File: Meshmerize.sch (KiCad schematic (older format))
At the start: 45 parts, among them M1 Motor_DC, M2 Motor_DC, SW1 SW_Push, U1 LM324, U2 ESP32-DEVKITC-32D, U3 TCRT5000, U4 TCRT5000, U5 MT3608, U6 TCRT5000, U7 TCRT5000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

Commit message: Completed PCB Routing
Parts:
- removed SW1: SW_Push, Button_Switch_THT:SW_PUSH_6mm, symbol Switch:SW_Push
- added H1, H2, H3, H4: MountingHole, MountingHole:MountingHole_2.2mm_M2, symbol Mechanical:MountingHole
- added J1, J2: Conn_01x19_Male, Connector_PinHeader_2.54mm:PinHeader_1x19_P2.54mm_Vertical, symbol Connector:Conn_01x19_Male
- added J3: Conn_01x04_Female, Connector_PinSocket_2.54mm:PinSocket_1x04_P2.54mm_Vertical, symbol Connector:Conn_01x04_Female
- added S2: MPB04-2C33-S-D, MPB04-2C33-S-D:SW_MPB04-2C33-S-D, symbol Meshmerize-rescue:MPB04-2C33-S-D-MPB04-2C33-S-D
- D6: symbol SS34:SS34 -> Meshmerize-rescue:SS34-SS34
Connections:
- net labels added: SCL_OLED, SDA_OLED
- wire segments 162 -> 201
- no-connect marks 22 -> 4

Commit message: Optimized schematics, routing and performed clean up
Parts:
- U5: symbol Regulator_Switching:MT3608 -> Meshmerize-rescue:MT3608-Regulator_Switching
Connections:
- wire segments 201 -> 203
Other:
- note added: "Buffer Op. Amplifiers - IC LM 324"
- note added: "Debug Switch"
- note added: "Indication LEDs"
- note added: "MCU - ESP 32"
- note added: "MT3608 - Boost StepUp Voltage Reg"
- note added: "Meshmerize"
- note added: "Motor Driver - TB6612FNG"
- note added: "Mounting Holes"
- note added: "OLED Port"
- note added: "Power Switch"
- note added: "TCRT5000 - IR TX RX"
- note removed: "LM342_Op-Amp\n"
- note removed: "POWER_CIRCUITARY\n"
- note removed: "TB6612FNG_Motor_Driver\n\n"
- moved on the sheet: BT2, C1, C2, D1, D2, D3, D4, D5, D6, H1, H2, H3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

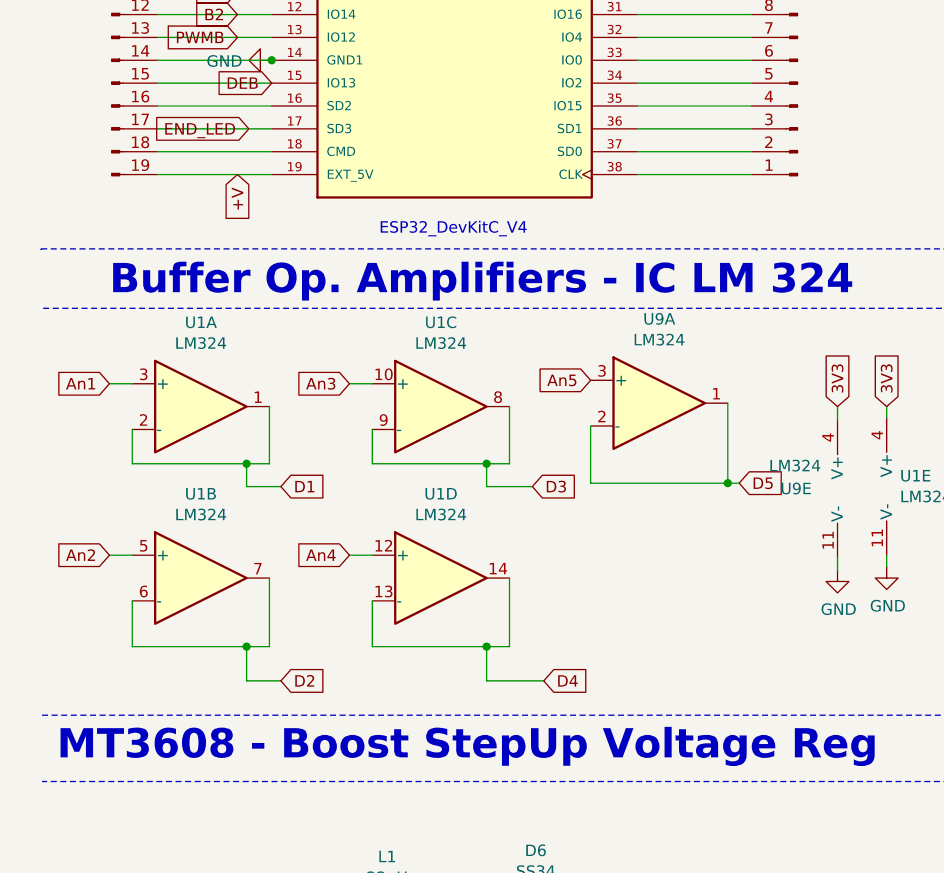
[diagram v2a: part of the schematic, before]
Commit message: Added R-Pot for LSA sensitivity, jumper to power ESP32 using inbuilt regulator, minor optimizations
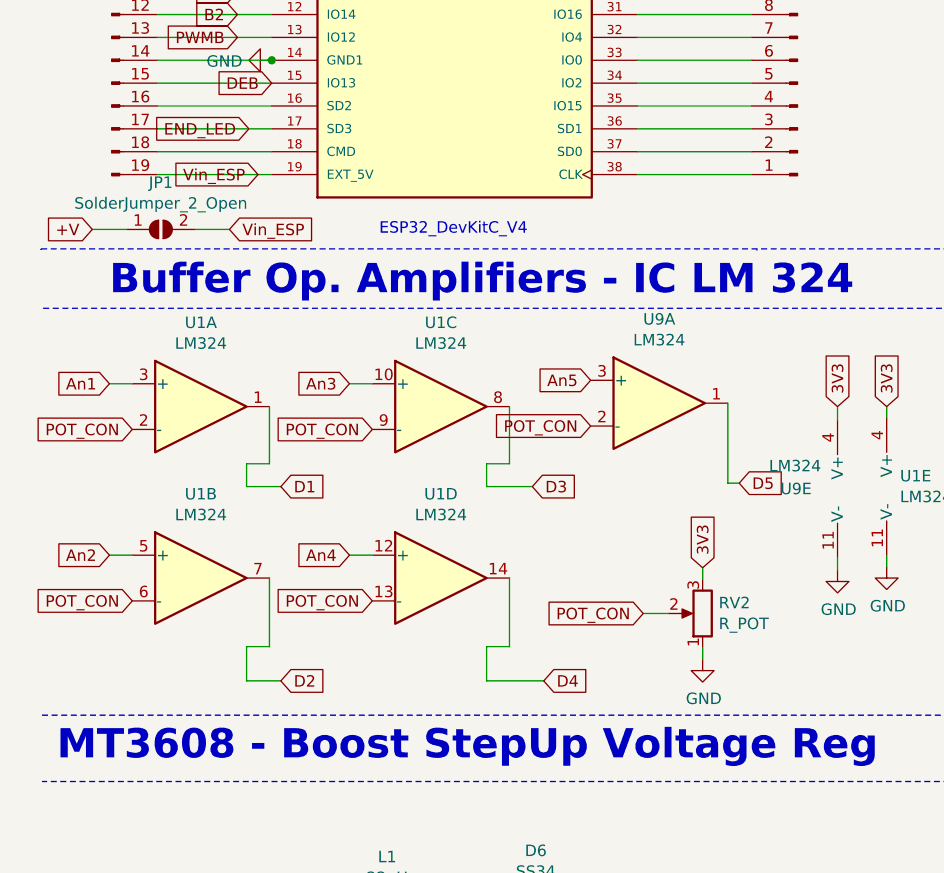
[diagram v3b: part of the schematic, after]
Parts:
- added JP1: SolderJumper_2_Open, Jumper:SolderJumper-2_P1.3mm_Open_Pad1.0x1.5mm, symbol Jumper:SolderJumper_2_Open
- added RV2: R_POT, 3296W-1-202LF:TRIM_3296W-1-202LF, symbol Device:R_POT
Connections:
- net +V: now also JP1.1 (A); no longer J1.19 (Pin_19), U2.19 (EXT_5V)
- net 3V3: now also RV2.3
- net D1: no longer U1.2 (-)
- net D2: no longer U1.6 (-)
- net D3: no longer U1.9 (-)
- net D4: no longer U1.13 (-)
- net D5: no longer U9.2 (-)
- net GND: now also RV2.1
- new net POT_CON: RV2.2, U1.13 (-), U1.2 (-), U1.6 (-), U1.9 (-), U9.2 (-)
- new net Vin_ESP: J1.19 (Pin_19), JP1.2 (B), U2.19 (EXT_5V)
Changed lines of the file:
@@
 $EndComp
-Wire Wire Line
-	865  4185 865  4335
-Wire Wire Line
-	865  4335 1365 4335
 Wire Wire Line
 	1465 4335 1465 4085
 Wire Wire Line
-	1915 4185 1915 4335
-Wire Wire Line
-	1915 4335 2415 4335
-Wire Wire Line
 	2515 4335 2515 4085
 Wire Wire Line
 	1465 4835 1465 5135
 Wire Wire Line
-	865  5135 865  4935
-Wire Wire Line
 	2515 4835 2515 5135
 Wire Wire Line
 	2515 5135 2415 5135
-Wire Wire Line
-	1915 5135 1915 4935
 $Comp
 L power:GND #PWR0120
@@
 Wire Wire Line
 	2415 4435 2615 4435
-Connection ~ 2415 4335
 Wire Wire Line
 	2415 4335 2515 4335
@@
 Wire Wire Line
 	1365 4435 1515 4435
-Connection ~ 1365 4335
 Wire Wire Line
 	1365 4335 1465 4335
@@
 	1365 5285 1515 5285
 Wire Wire Line
-	865  5135 1365 5135
-Connection ~ 1365 5135
-Wire Wire Line
 	1365 5135 1465 5135
 Wire Wire Line
@@
 Wire Wire Line
 	2415 5285 2665 5285
-Connection ~ 2415 5135
-Wire Wire Line
-	2415 5135 1915 5135
 Text GLabel 765  3985 0    50   Input ~ 0
 An1
@@
 $EndComp
 Wire Wire Line
-	2870 4170 2870 4420
-Wire Wire Line
-	2870 4420 3470 4420
-Wire Wire Line
 	3470 4420 3470 4070
 Text GLabel 2870 3970 0    50   Input ~ 0
@@
 Wire Wire Line
 	3470 4420 3520 4420
-Connection ~ 3470 4420
 $Comp
 L power:GND #PWR02
@@
 	975  2770 1475 2770
 Wire Wire Line
-	975  3070 1475 3070
-Wire Wire Line
 	975  1270 1475 1270
 $Comp
@@
 Text GLabel 1475 2670 0    50   Input ~ 0
 DEB
-Text GLabel 1325 3070 3    50   Input ~ 0
+Text GLabel 690  3310 0    50   Input ~ 0
 +V
 Text GLabel 1375 1270 1    50   Input ~ 0
@@
 Wire Notes Line
 	8295 2490 11200 2490
+$Comp
+L Device:R_POT RV2
+U 1 1 6199FDC2
+P 3360 4990
+F 0 "RV2" H 3290 4944 50  0000 R CNN
+F 1 "R_POT" H 3290 5035 50  0000 R CNN
+F 2 "3296W-1-202LF:TRIM_3296W-1-202LF" H 3360 4990 50  0001 C CNN
+F 3 "~" H 3360 4990 50  0001 C CNN
+	1    3360 4990
+	-1   0    0    1
+$EndComp
+Text GLabel 3100 4990 0    50   Input ~ 0
+POT_CON
+Wire Wire Line
+	3210 4990 3100 4990
+$Comp
+L power:GND #PWR0107
+U 1 1 619F79F0
+P 3360 5190
+F 0 "#PWR0107" H 3360 4940 50  0001 C CNN
+F 1 "GND" H 3365 5017 50  0000 C CNN
+F 2 "" H 3360 5190 50  0001 C CNN
+F 3 "" H 3360 5190 50  0001 C CNN
+	1    3360 5190
+	1    0    0    -1
+$EndComp
+Wire Wire Line
+	3360 5140 3360 5190
+Wire Wire Line
+	3360 4840 3360 4790
+Text GLabel 3360 4790 1    50   Input ~ 0
+3V3
+Text GLabel 2870 4170 0    50   Input ~ 0
+POT_CON
+Text GLabel 1915 4185 0    50   Input ~ 0
+POT_CON
+Text GLabel 865  4185 0    50   Input ~ 0
+POT_CON
+Text GLabel 865  4935 0    50   Input ~ 0
+POT_CON
+Text GLabel 1915 4935 0    50   Input ~ 0
+POT_CON
+Text GLabel 1290 3310 2    50   Input ~ 0
+Vin_ESP
+Text GLabel 1415 3070 0    50   Input ~ 0
+Vin_ESP
+Wire Wire Line
+	975  3070 1475 3070
+$Comp
+L Jumper:SolderJumper_2_Open JP1
+U 1 1 61B9BE6D
+P 990 3310
+F 0 "JP1" H 990 3515 50  0000 C CNN
+F 1 "SolderJumper_2_Open" H 990 3424 50  0000 C CNN
+F 2 "Jumper:SolderJumper-2_P1.3mm_Open_Pad1.0x1.5mm" H 990 3310 50  0001 C CNN
+F 3 "~" H 990 3310 50  0001 C CNN
+	1    990  3310
+	1    0    0    -1
+$EndComp
+Wire Wire Line
+	1140 3310 1290 3310
+Wire Wire Line
+	690  3310 840  3310
 $EndSCHEMATC

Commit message: Added 3D Files
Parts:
- C1, C2: footprint Capacitor_SMD:C_1812_4532Metric -> Capacitor_SMD:C_0805_2012Metric
- L1: footprint Inductor_SMD:L_10.4x10.4_H4.8 -> Inductor_SMD:L_12x12mm_H6mm
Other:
- note added: "MAZEBLAZE"
- note removed: "Meshmerize"
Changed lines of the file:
@@
 F 0 "L1" V 2170 6245 50  0000 C CNN
 F 1 "22uH" V 2079 6245 50  0000 C CNN
-F 2 "Inductor_SMD:L_10.4x10.4_H4.8" H 1980 6245 50  0001 C CNN
+F 2 "Inductor_SMD:L_12x12mm_H6mm" H 1980 6245 50  0001 C CNN
 F 3 "~" H 1980 6245 50  0001 C CNN
 	1    1980 6245
@@
 F 0 "C1" H 1595 7141 50  0000 L CNN
 F 1 "22uF" H 1595 7050 50  0000 L CNN
-F 2 "Capacitor_SMD:C_1812_4532Metric" H 1518 6945 50  0001 C CNN
+F 2 "Capacitor_SMD:C_0805_2012Metric" H 1518 6945 50  0001 C CNN
 F 3 "~" H 1480 7095 50  0001 C CNN
 	1    1480 7095
@@
 F 0 "C2" H 3595 6891 50  0000 L CNN
 F 1 "22uF" H 3595 6800 50  0000 L CNN
-F 2 "Capacitor_SMD:C_1812_4532Metric" H 3518 6695 50  0001 C CNN
+F 2 "Capacitor_SMD:C_0805_2012Metric" H 3518 6695 50  0001 C CNN
 F 3 "~" H 3480 6845 50  0001 C CNN
 	1    3480 6845
@@
 $EndComp
 Text Notes 4635 340  0    207  ~ 41
-Meshmerize
+MAZEBLAZE
 Text Notes 1645 710  0    128  ~ 26
 MCU - ESP 32

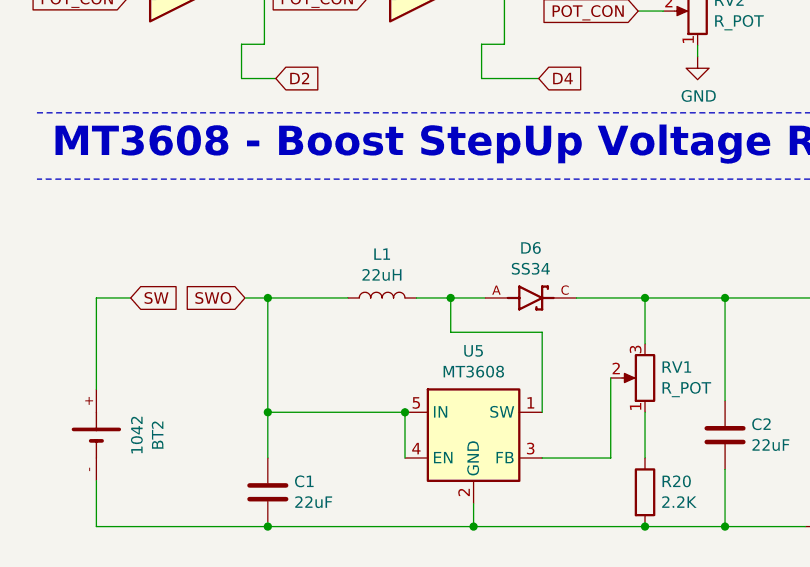
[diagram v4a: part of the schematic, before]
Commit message: Fixed errors, optlized routing
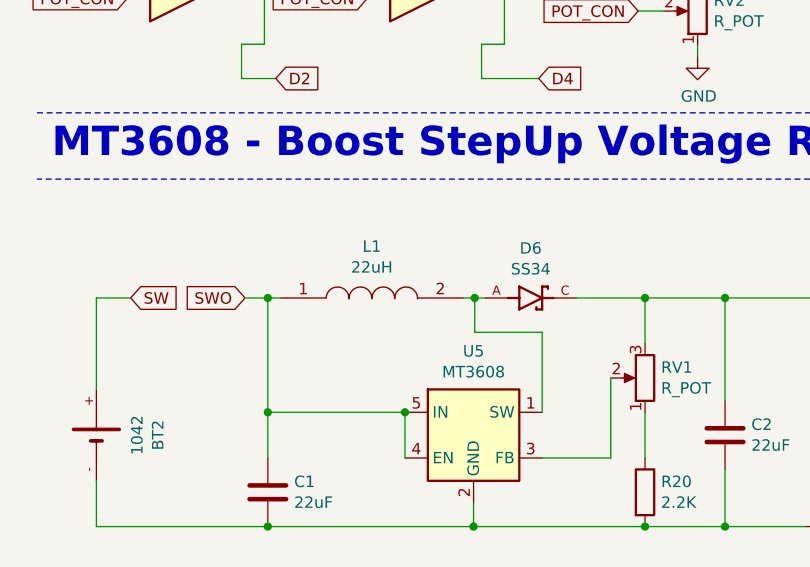
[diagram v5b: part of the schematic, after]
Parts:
- removed L1: 22uH, Inductor_SMD:L_12x12mm_H6mm, symbol Device:L
- added L1: 22uH, CDRH104RNP-220NC:INDPM102100X400N, symbol CDRH104RNP-220NC:CDRH104RNP-220NC
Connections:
- net SWO: now also L1.1
- net at D6.A, U5.1 (SW): now also L1.2
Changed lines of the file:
@@
-$EndComp
-$Comp
-L Device:L L1
-U 1 1 61935A19
-P 1980 6245
-F 0 "L1" V 2170 6245 50  0000 C CNN
-F 1 "22uH" V 2079 6245 50  0000 C CNN
-F 2 "Inductor_SMD:L_12x12mm_H6mm" H 1980 6245 50  0001 C CNN
-F 3 "~" H 1980 6245 50  0001 C CNN
-	1    1980 6245
-	0    -1   -1   0
 $EndComp
 $Comp
@@
 	1480 6245 1480 6745
 Wire Wire Line
-	2130 6245 2280 6245
-Wire Wire Line
 	2830 6245 3130 6245
-Wire Wire Line
-	1480 6245 1830 6245
 Wire Wire Line
 	2080 6945 2080 6745
@@
 	2680 6745 2680 6395
 Wire Wire Line
-	2680 6395 2280 6395
-Wire Wire Line
-	2280 6395 2280 6245
-Connection ~ 2280 6245
-Wire Wire Line
-	2280 6245 2430 6245
+	2680 6395 2385 6395
 Wire Wire Line
 	2380 7145 2380 7245
@@
 Wire Wire Line
 	1380 6245 1480 6245
-Connection ~ 1480 6245
 $Comp
 L Connector:Conn_01x04_Female J3
@@
 Wire Wire Line
 	690  3310 840  3310
+$Comp
+L CDRH104RNP-220NC:CDRH104RNP-220NC L1
+U 1 1 6199AF4F
+P 1535 6245
+F 0 "L1" H 1935 6470 50  0000 C CNN
+F 1 "22uH" H 1935 6379 50  0000 C CNN
+F 2 "CDRH104RNP-220NC:INDPM102100X400N" H 2185 6295 50  0001 L CNN
+F 3 "http://products.sumida.com/products/pdf/CDRH104R.pdf" H 2185 6195 50  0001 L CNN
+F 4 "Fixed Inductors 22uH 2.5A" H 2185 6095 50  0001 L CNN "Description"
+F 5 "4" H 2185 5995 50  0001 L CNN "Height"
+F 6 "Sumida" H 2185 5895 50  0001 L CNN "Manufacturer_Name"
+F 7 "CDRH104RNP-220NC" H 2185 5795 50  0001 L CNN "Manufacturer_Part_Number"
+F 8 "851-CDRH104RNP-220NC" H 2185 5695 50  0001 L CNN "Mouser Part Number"
+F 9 "https://www.mouser.co.uk/ProductDetail/Sumida/CDRH104RNP-220NC?qs=iXFGfj0UVr7lF4yqUlpBKQ%3D%3D" H 2185 5595 50  0001 L CNN "Mouser Price/Stock"
+F 10 "CDRH104RNP-220NC" H 2185 5495 50  0001 L CNN "Arrow Part Number"
+F 11 "https://www.arrow.com/en/products/cdrh104rnp-220nc/sumida" H 2185 5395 50  0001 L CNN "Arrow Price/Stock"
+	1    1535 6245
+	1    0    0    -1
+$EndComp
+Wire Wire Line
+	1535 6245 1480 6245
+Connection ~ 1480 6245
+Wire Wire Line
+	2335 6245 2385 6245
+Wire Wire Line
+	2385 6395 2385 6245
+Connection ~ 2385 6245
+Wire Wire Line
+	2385 6245 2430 6245
 $EndSCHEMATC
